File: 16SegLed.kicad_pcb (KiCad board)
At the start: 2 copper layers, 99.9 x 79.6 mm, 56 parts, among them J1 Conn_01x10, J2 Conn_01x10, J3 Conn_01x10, J4 Conn_01x06_Socket, J5 Conn_01x04_Pin, J6 Conn_01x04_Pin, Q1 BSS138, Q2 BSS138, SW1 SW_Push, SW2 SW_Push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

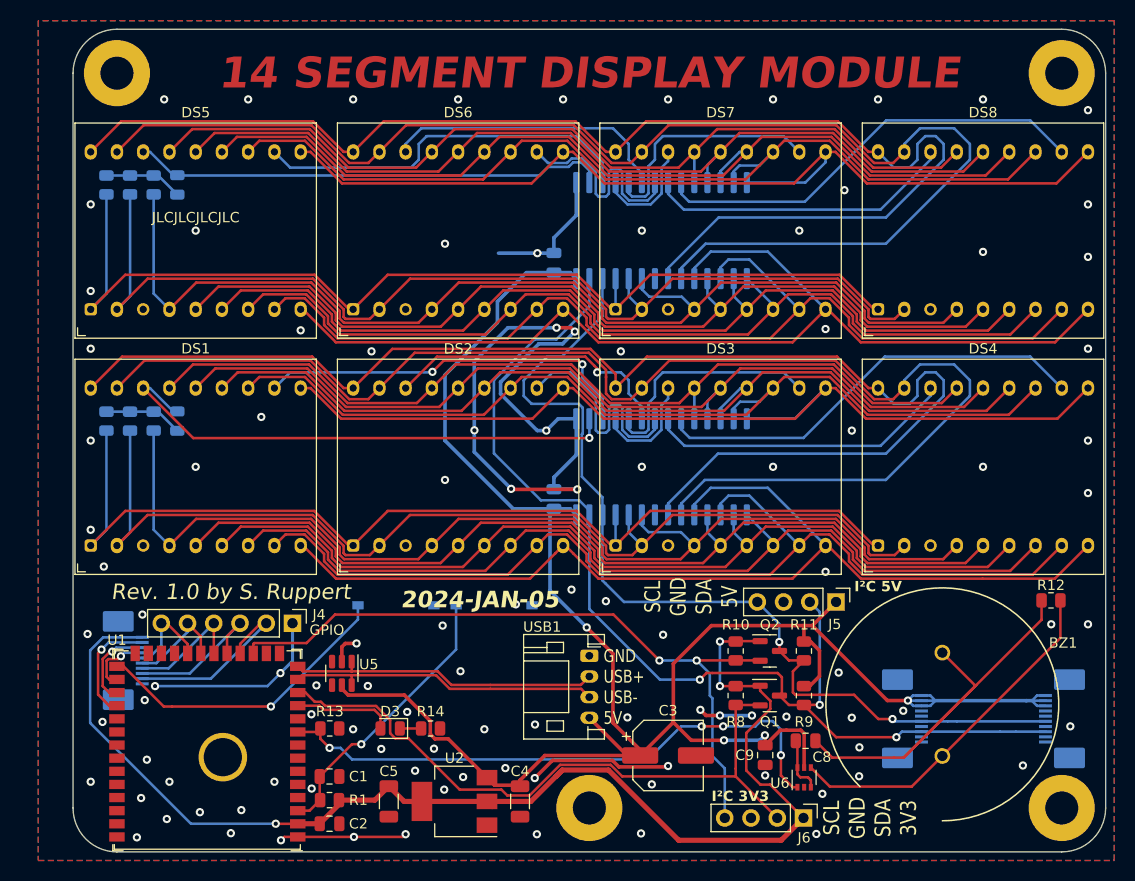
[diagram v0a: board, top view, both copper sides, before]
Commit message: Flipped all SMD components to back side
- Exceptions: large electrolytic capacitor, optional GPIO connector
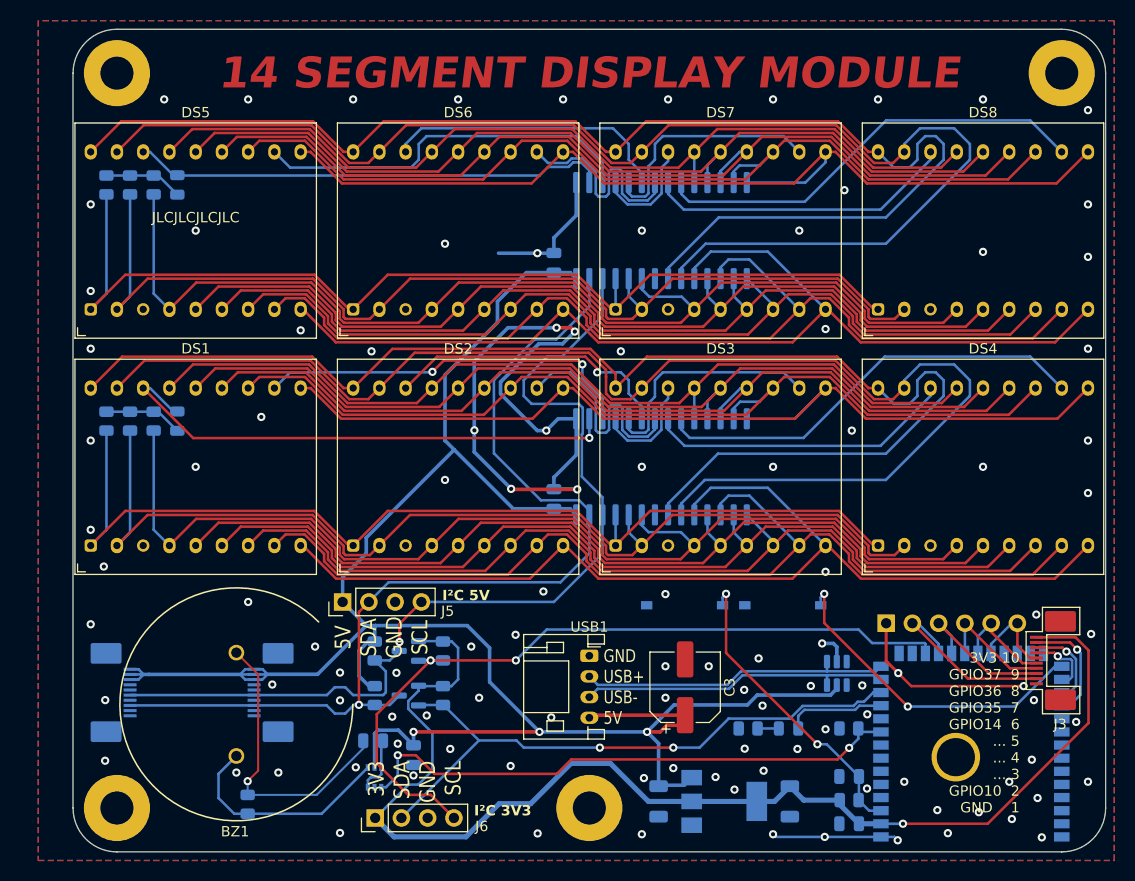
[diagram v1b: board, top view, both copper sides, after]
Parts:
- C1, C2, C4, C5, C8, C9, D3, H3, H4, J4, Q1, Q2, R1, R10, R11, R12, R13, R14, R8, R9, U1, U2, U5, U6: moved to B.Cu
- J3: moved to F.Cu
- moved H3 91.4 mm to (105.1, 168.6), turned to 180 degrees
- moved J3 86.5 mm to (194.1, 154.3)
- moved R12 80.2 mm to (117.7, 168.2), turned to 90 degrees
- moved J1 76.6 mm to (106.3, 157.4)
- moved J2 76.6 mm to (118.4, 157.4)
- moved U1 73.9 mm to (187.8, 163.1), turned to 0 degrees
- moved BZ1 68.3 mm to (116.6, 158.5)
- moved J4 57.5 mm to (179.5, 150.7)
- moved C1 50.3 mm to (175.9, 165.5), turned to 180 degrees
- moved C2 50.3 mm to (175.9, 170.1), turned to 180 degrees
- moved R1 50.3 mm to (175.9, 167.8), turned to 0 degrees
- moved R13 50.2 mm to (175.9, 160.9), turned to 180 degrees
- moved U5 47.9 mm to (174.8, 155.5)
- moved J5 47.8 mm to (126.9, 148.6), turned to 90 degrees
- moved C8 41.9 mm to (129.9, 162.1), turned to 180 degrees
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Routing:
- net GND: track 126.6 -> 107.6 mm, vias 108 -> 111
- net /BZ-: track 45.0 -> 28.8 mm, vias 0 -> 1
- net /BZ+: track 34.5 -> 21.7 mm
- net /SDA5V: track 106.3 -> 98.4 mm, vias 3 -> 1
- net /SCL3V3: track 69.4 -> 74.8 mm
- net /SDA3V3: track 63.9 -> 59.3 mm, vias 0 -> 2
- net +3V3: track 125.5 -> 121.5 mm, vias 3 -> 1
- net +5V: track 199.4 -> 203.1 mm, vias 4 -> 3
- net /SND: track 57.1 -> 54.1 mm, vias 4 -> 2
- net /BOOT: track 29.8 -> 32.0 mm, vias 1 -> 2
- net /CHIP_PU: track 27.5 -> 29.7 mm, vias 1 -> 2
- net /DisplayGroup0/SEG11: track 90.0 -> 89.0 mm
- net /SCL5V: track 92.5 -> 93.3 mm, vias 2 -> 1
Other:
- board text added: "2024-JAN-06"
- board text added: "3V3 10 GPIO37 9 GPIO36 8 GPIO35 7 GPIO14 6 ... 5 ... 4 ... 3 GPIO10 2 GND 1"
- board text added: "3V3 SDA GND SCL"
- board text added: "5V SDA GND SCL"
- board text added: "Rev. 1.0 Sascha Ruppert"
- board text added: "SCL G D 3"
- board text removed: "2024-JAN-05"
- board text removed: "3V3 IO37 ... IO35 IO14 ... IO10 GND"
- board text removed: "Rev. 1.0 by S. Ruppert"
- board text removed: "SCL GND SDA 3V3"

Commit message: Add QR code for repository @ github
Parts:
- added FID1: Fiducial, ProjectLibrary:QR-Code, B.Cu at (188.9, 112.7)
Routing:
- net GND: vias 111 -> 109
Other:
- board text added: "github.com/cawapy/14Segments"
